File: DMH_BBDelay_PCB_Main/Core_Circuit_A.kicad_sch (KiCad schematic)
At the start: 62 parts, among them Q3 J113, SW3 SW_SPDT, U1 TL074, U2 TL074, U3 V3205, U4 CD4046, U9 40106

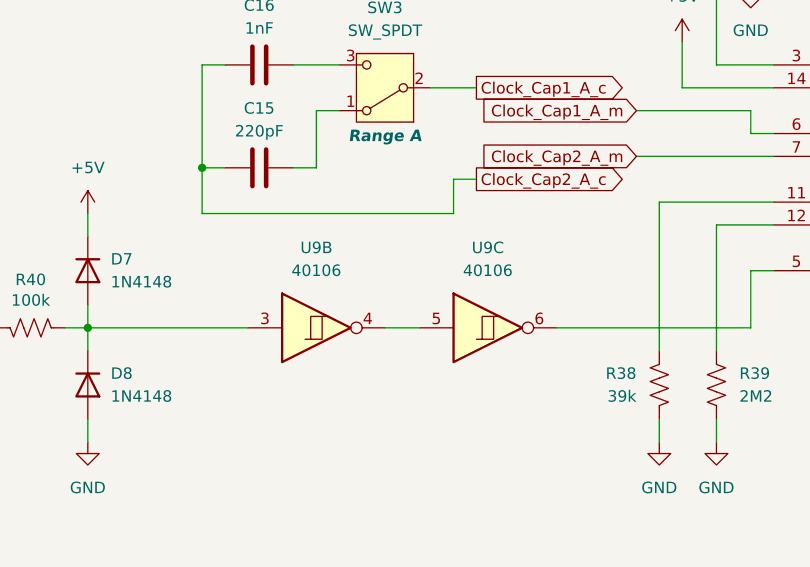
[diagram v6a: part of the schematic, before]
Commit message: Schmitt triggers added to Inhibt CV input paths
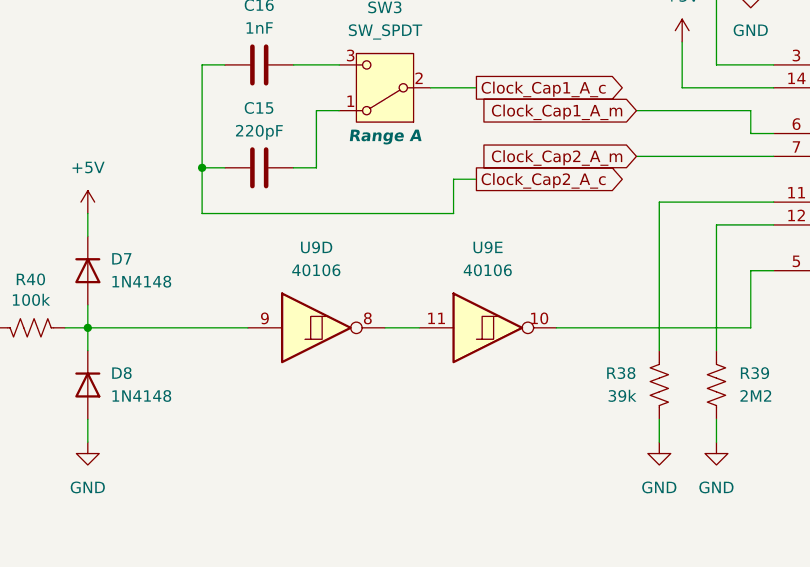
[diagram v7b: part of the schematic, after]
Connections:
- net at D7.2 (A), D8.1 (K), R40.2: now also U9.9; no longer U9.3
- net at U4.5 (Inh): now also U9.10; no longer U9.6
- new net: U9.11, U9.8
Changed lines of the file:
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@@
 		(lib_id "4xxx:40106")
 		(at 88.9 171.45 0)
-		(unit 2)
+		(unit 4)
 		(body_style 1)
 		(exclude_from_sim no)
@@
 			)
 		)
+		(property "Function" ""
+			(at 88.9 171.45 0)
+			(show_name no)
+			(do_not_autoplace no)
+			(effects
+				(font
+					(size 1.27 1.27)
+				)
+			)
+		)
 		(pin "3"
 		)
@@
 				(path "/58f4306d-5387-4983-bb08-41a2313fd315/7ad2d702-dfb7-4d49-a82d-34430dd5948f"
 					(reference "U9")
-					(unit 2)
+					(unit 4)
 				)
 			)
@@
 		(lib_id "4xxx:40106")
 		(at 107.95 171.45 0)
-		(unit 3)
+		(unit 5)
 		(body_style 1)
 		(exclude_from_sim no)
@@
 			)
 		)
+		(property "Function" ""
+			(at 107.95 171.45 0)
+			(show_name no)
+			(do_not_autoplace no)
+			(effects
+				(font
+					(size 1.27 1.27)
+				)
+			)
+		)
 		(pin "3"
 		)
@@
 				(path "/58f4306d-5387-4983-bb08-41a2313fd315/7ad2d702-dfb7-4d49-a82d-34430dd5948f"
 					(reference "U9")
-					(unit 3)
-				)
-			)
+					(unit 5)
+				)
+			)

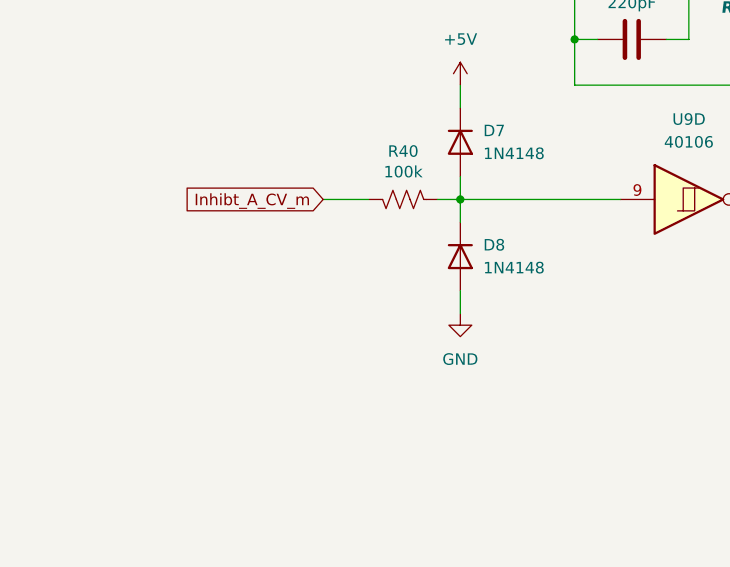
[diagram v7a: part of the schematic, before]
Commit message: Added TRS jacks to IO page
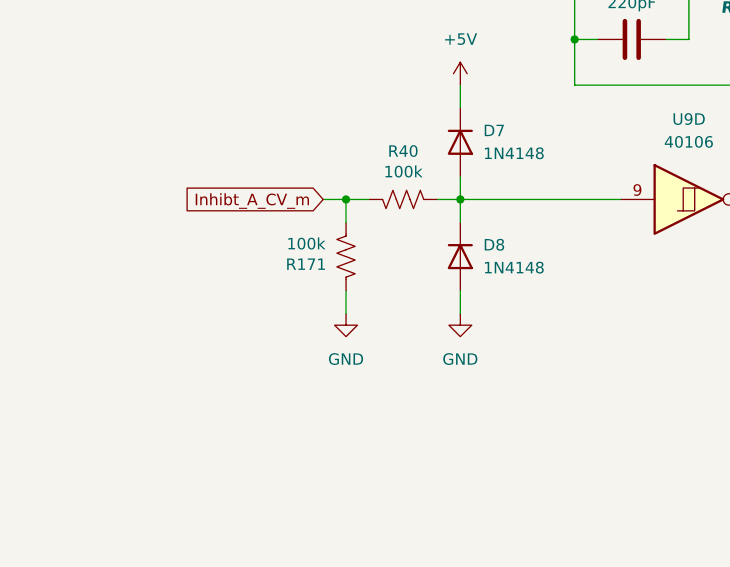
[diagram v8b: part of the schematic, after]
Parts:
- added R171: 100k, Resistor_THT:R_Axial_DIN0207_L6.3mm_D2.5mm_P7.62mm_Horizontal, symbol Device:R_US
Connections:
- net GND: now also R171.1
- net Inhibt_A_CV_m: now also R171.2
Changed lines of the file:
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@@
 	)
 	(junction
+		(at 50.8 171.45)
+		(diameter 0)
+		(color 0 0 0 0)
+	)
+	(junction
 		(at 228.6 95.25)
 		(diameter 0)
@@
 	(wire
 		(pts
-			(xy 48.26 171.45) (xy 53.34 171.45)
+			(xy 48.26 171.45) (xy 50.8 171.45)
 		)
 		(stroke
@@
 	(wire
 		(pts
+			(xy 50.8 171.45) (xy 53.34 171.45)
+		)
+		(stroke
+			(width 0)
+			(type default)
+		)
+	)
+	(wire
+		(pts
 			(xy 212.09 152.4) (xy 214.63 152.4)
 		)
@@
 	(wire
 		(pts
+			(xy 50.8 181.61) (xy 50.8 184.15)
+		)
+		(stroke
+			(width 0)
+			(type default)
+		)
+	)
+	(wire
+		(pts
 			(xy 124.46 147.32) (xy 137.16 147.32)
 		)
@@
 	(wire
 		(pts
+			(xy 50.8 171.45) (xy 50.8 173.99)
+		)
+		(stroke
+			(width 0)
+			(type default)
+		)
+	)
+	(wire
+		(pts
 			(xy 190.5 69.85) (xy 201.93 69.85)
 		)
@@
 	)
 	(symbol
+		(lib_id "Device:R_US")
+		(at 50.8 177.8 0)
+		(mirror x)
+		(unit 1)
+		(body_style 1)
+		(exclude_from_sim no)
+		(in_bom yes)
+		(on_board yes)
+		(in_pos_files yes)
+		(dnp no)
+		(property "Reference" "R171"
+			(at 46.355 178.689 0)
+			(show_name no)
+			(do_not_autoplace no)
+			(effects
+				(font
+					(size 1.27 1.27)
+				)
+			)
+		)
+		(property "Value" "100k"
+			(at 46.355 176.403 0)
+			(show_name no)
+			(do_not_autoplace no)
+			(effects
+				(font
+					(size 1.27 1.27)
+				)
+			)
+		)
+		(property "Footprint" "Resistor_THT:R_Axial_DIN0207_L6.3mm_D2.5mm_P7.62mm_Horizontal"
+			(at 51.816 177.546 90)
+			(hide yes)
+			(show_name no)
+			(do_not_autoplace no)
+			(effects
+				(font
+					(size 1.27 1.27)
+				)
+			)
+		)
+		(property "Datasheet" ""
+			(at 50.8 177.8 0)
+			(hide yes)
+			(show_name no)
+			(do_not_autoplace no)
+			(effects
+				(font
+					(size 1.27 1.27)
+				)
+			)
+		)
+		(property "Description" "Resistor, US symbol"
+			(at 50.8 177.8 0)
+			(hide yes)
+			(show_name no)
+			(do_not_autoplace no)
+			(effects
+				(font
+					(size 1.27 1.27)
+				)
+			)
+		)
+		(pin "2"
+		)
+		(pin "1"
+		)
+		(instances
+			(project "DMH_BBDelay_PCB_Main"
+				(path "/58f4306d-5387-4983-bb08-41a2313fd315/7ad2d702-dfb7-4d49-a82d-34430dd5948f"
+					(reference "R171")
+					(unit 1)
+				)
+			)
+		)
+	)
+	(symbol
 		(lib_id "Diode:1N4148")
 		(at 63.5 177.8 270)
@@
 					(unit 1)
 				)
+			)
+		)
+	)
+	(symbol
+		(lib_id "power:GND")
+		(at 50.8 184.15 0)
+		(unit 1)
+		(body_style 1)
+		(exclude_from_sim no)
+		(in_bom yes)
+		(on_board yes)
+		(in_pos_files yes)
+		(dnp no)
+		(fields_autoplaced yes)
+		(property "Reference" "#PWR0198"
+			(at 50.8 190.5 0)
+			(hide yes)
+			(show_name no)
+			(do_not_autoplace no)
+			(effects
+				(font
+					(size 1.27 1.27)
+				)
+			)
+		)
+		(property "Value" "GND"
+			(at 50.8 189.23 0)
+			(show_name no)
+			(do_not_autoplace no)
+			(effects
+				(font
+					(size 1.27 1.27)
+				)
+			)
+		)
+		(property "Footprint" ""
+			(at 50.8 184.15 0)
+			(hide yes)
+			(show_name no)
+			(do_not_autoplace no)
+			(effects
+				(font
+					(size 1.27 1.27)
+				)
+			)
+		)
+		(property "Datasheet" ""
+			(at 50.8 184.15 0)
+			(hide yes)
+			(show_name no)
+			(do_not_autoplace no)
+			(effects
+				(font
+					(size 1.27 1.27)
+				)
+			)
+		)
+		(property "Description" "Power symbol creates a global label with name \"GND\" , ground"
+			(at 50.8 184.15 0)
+			(hide yes)
+			(show_name no)
+			(do_not_autoplace no)
+			(effects
+				(font
+					(size 1.27 1.27)
+				)
+			)
+		)
+		(pin "1"
+		)
+		(instances
+			(project "DMH_BBDelay_PCB_Main"
+				(path "/58f4306d-5387-4983-bb08-41a2313fd315/7ad2d702-dfb7-4d49-a82d-34430dd5948f"
+					(reference "#PWR0198")
+					(unit 1)
+				)
